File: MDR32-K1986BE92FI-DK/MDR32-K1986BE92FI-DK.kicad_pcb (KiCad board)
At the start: 2 copper layers, 69.6 x 21.4 mm, 57 parts, among them J1 Conn_PROBE, J2 PIN_A, J3 SYS_A, J4 USB_C_Receptacle_USB2.0_16P, J5 PIN_B, J6 SYS_B, Q1 AO3401A, SW1 IT-1181, SW2 SW_DIP_x02, SW3 IT-1181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

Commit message: fix position
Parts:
- moved R1 95.9 mm to (154.5, 134.9)
- moved R2 72.1 mm to (128.7, 134.8)
- moved SW1 57.9 mm to (145.4, 130.8)
- moved Q1 54.1 mm to (147.2, 136.4)
- moved U1 53.5 mm to (125.9, 104.9)
- moved D3 40.0 mm to (128.7, 137.9)
- moved C2 39.4 mm to (118.2, 119.3)
- moved C1 39.2 mm to (118.3, 114.7)
- moved D1 38.3 mm to (128.2, 113.3)
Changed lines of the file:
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@@
 	(footprint "Capacitor_SMD:C_0805_2012Metric"
 		(layer "F.Cu")
-		(at 80.39 104.995)
+		(at 118.35 114.67)
 		(descr "Capacitor SMD 0805 (2012 Metric), square (rectangular) end terminal, IPC_7351 nominal, (Body size source: IPC-SM-782 page 76, https://www.pcb-3d.com/wordpress/wp-content/uploads/ipc-sm-782a_amendment_1_and_2.pdf, https://docs.google.com/spreadsheets/d/1BsfQQcO9C6DZCsRaXUlFlo91Tg2WpOkGARC1WS5S8t0/edit?usp=sharing), generated with kicad-footprint-generator")
 		(tags "capacitor")
@@
 	(footprint "Resistor_SMD:R_0603_1608Metric"
 		(layer "F.Cu")
-		(at 68.14 95.725)
+		(at 128.685 134.81)
 		(descr "Resistor SMD 0603 (1608 Metric), square (rectangular) end terminal, IPC_7351 nominal, (Body size source: IPC-SM-782 page 72, https://www.pcb-3d.com/wordpress/wp-content/uploads/ipc-sm-782a_amendment_1_and_2.pdf), generated with kicad-footprint-generator")
 		(tags "resistor")
@@
 	(footprint "Package_TO_SOT_SMD:SOT-223-3_TabPin2"
 		(layer "F.Cu")
-		(at 76.35 125)
+		(at 125.93 104.9)
 		(descr "module CMS SOT223 4 pins")
 		(tags "CMS SOT")
@@
 	(footprint "Button_Switch_SMD:SW_SPST_CK_RS282G05A3"
 		(layer "F.Cu")
-		(at 88.12 122.095)
+		(at 145.39 130.82)
 		(descr "https://www.mouser.com/ds/2/60/RS-282G05A-SM_RT-1159762.pdf")
 		(tags "SPST button tactile switch")
@@
 		(locked yes)
 		(layer "F.Cu")
-		(at 20.72 27.73 -90)
+		(at 20.715 27.73 -90)
 		(descr "USB 2.0 Type C Receptacle, GCT, 16P, top mounted, horizontal, 5A: https://gct.co/files/drawings/usb4105.pdf")
 		(tags "USB C Type-C Receptacle SMD USB 2.0 16P 16C USB4105-15-A USB4105-15-A-060 USB4105-15-A-120 USB4105-GF-A USB4105-GF-A-060 USB4105-GF-A-120")
@@
 	(footprint "Resistor_SMD:R_0603_1608Metric"
 		(layer "F.Cu")
-		(at 68.14 93.215)
+		(at 154.535 134.9)
 		(descr "Resistor SMD 0603 (1608 Metric), square (rectangular) end terminal, IPC_7351 nominal, (Body size source: IPC-SM-782 page 72, https://www.pcb-3d.com/wordpress/wp-content/uploads/ipc-sm-782a_amendment_1_and_2.pdf), generated with kicad-footprint-generator")
 		(tags "resistor")
@@
 	(footprint "Capacitor_SMD:C_0805_2012Metric"
 		(layer "F.Cu")
-		(at 80.39 108.005)
+		(at 118.16 119.29)
 		(descr "Capacitor SMD 0805 (2012 Metric), square (rectangular) end terminal, IPC_7351 nominal, (Body size source: IPC-SM-782 page 76, https://www.pcb-3d.com/wordpress/wp-content/uploads/ipc-sm-782a_amendment_1_and_2.pdf, https://docs.google.com/spreadsheets/d/1BsfQQcO9C6DZCsRaXUlFlo91Tg2WpOkGARC1WS5S8t0/edit?usp=sharing), generated with kicad-footprint-generator")
 		(tags "capacitor")
@@
 	(footprint "LED_SMD:LED_0805_2012Metric"
 		(layer "F.Cu")
-		(at 89.29 131.34)
+		(at 128.74 137.9)
 		(descr "LED SMD 0805 (2012 Metric), square (rectangular) end terminal, IPC_7351 nominal, (Body size source: https://docs.google.com/spreadsheets/d/1BsfQQcO9C6DZCsRaXUlFlo91Tg2WpOkGARC1WS5S8t0/edit?usp=sharing), generated with kicad-footprint-generator")
 		(tags "LED")
@@
 	(footprint "Diode_SMD:D_SOD-123"
 		(layer "F.Cu")
-		(at 90.785 105.165)
+		(at 128.21 113.26)
 		(descr "SOD-123")
 		(tags "SOD-123")
@@
 	(footprint "Package_TO_SOT_SMD:SOT-23"
 		(layer "F.Cu")
-		(at 96.83 116.555)
+		(at 147.1725 136.41)
 		(descr "SOT, 3 Pin (JEDEC TO-236 Var AB https://www.jedec.org/document_search?search_api_views_fulltext=TO-236), generated with kicad-footprint-generator ipc_gullwing_generator.py")
 		(tags "SOT TO_SOT_SMD")

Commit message: update footprints
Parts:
- J1: footprint Connector_PinHeader_2.54mm:PinHeader_1x04_P2.54mm_Vertical -> Connector_PinHeader_2.54mm:PinHeader_1x04_P2.54mm_Horizontal
- SW1, SW3: footprint Button_Switch_SMD:SW_SPST_CK_RS282G05A3 -> Button_Switch_SMD:SW_SPST_B3U-1000P

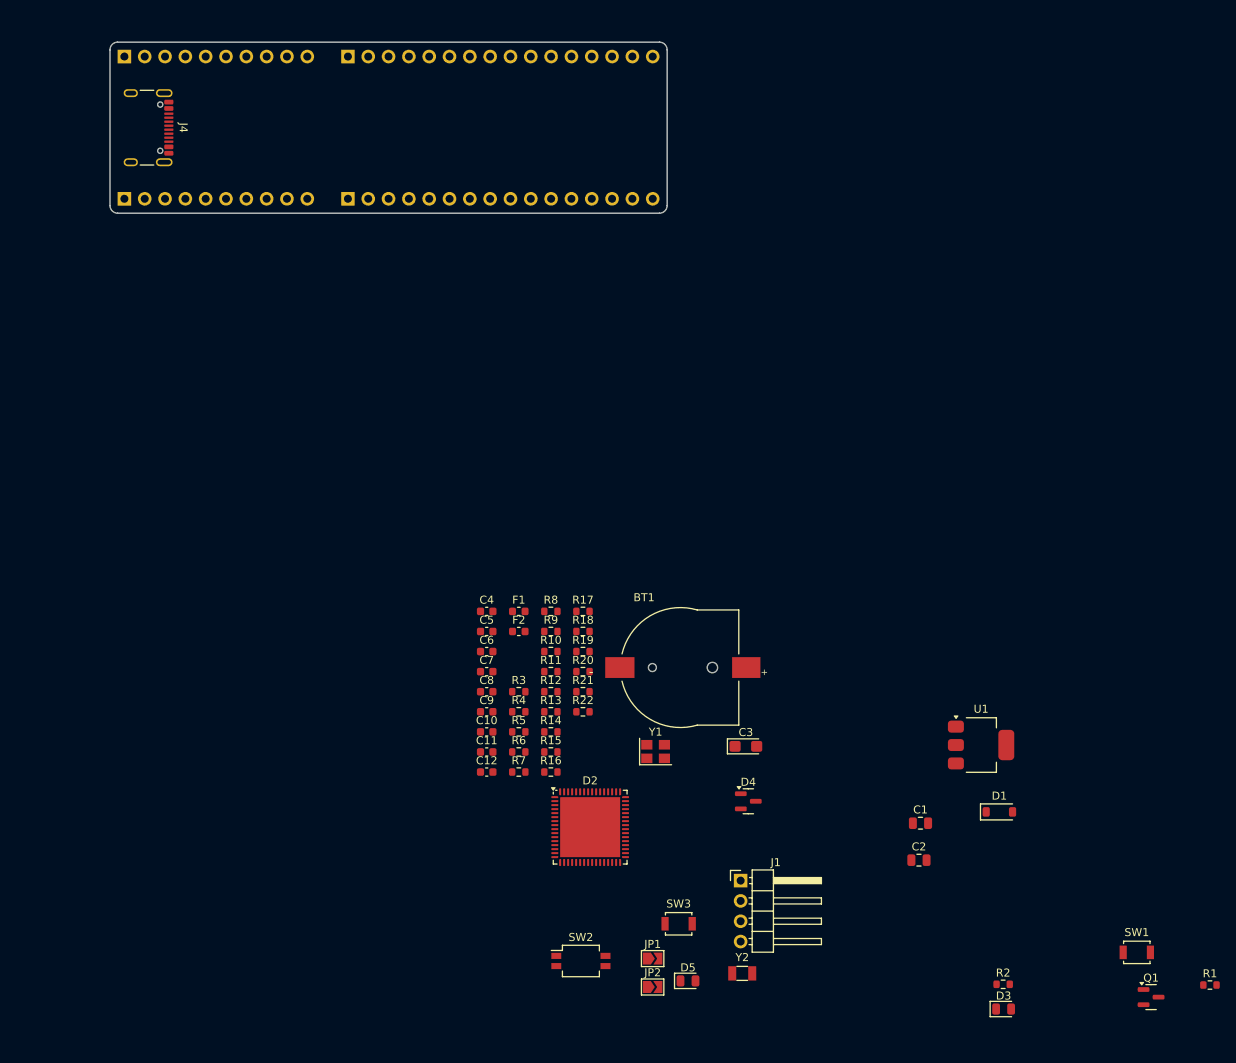
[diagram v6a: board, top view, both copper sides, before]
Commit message: position SW pinout
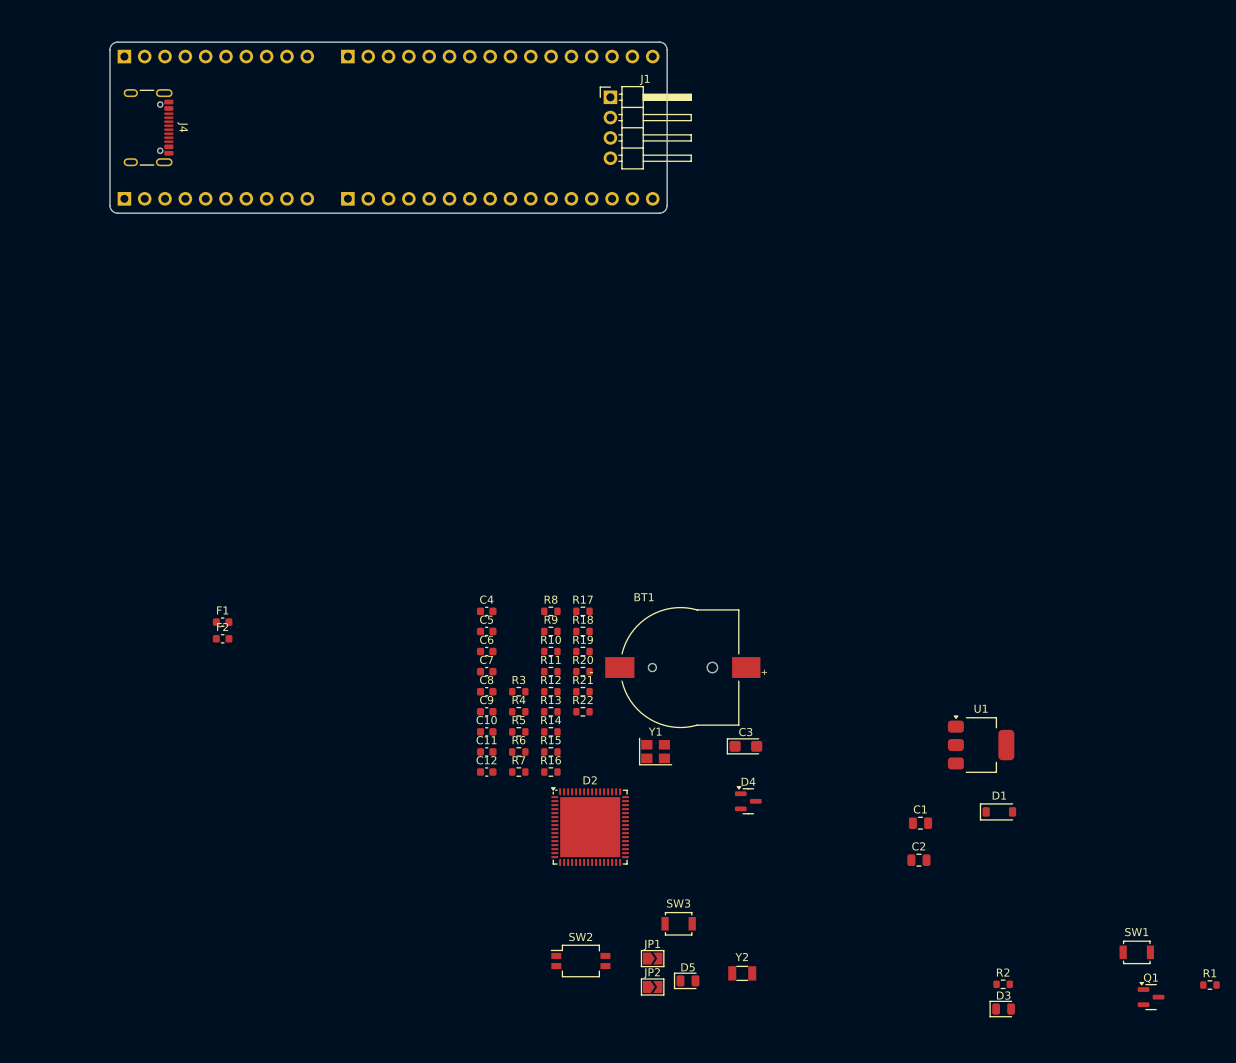
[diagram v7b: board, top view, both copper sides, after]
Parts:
- moved J1 99.3 mm to (79.6, 23.9)
- moved F1 37.0 mm to (31.1, 89.5)
- moved F2 37.0 mm to (31.1, 91.6)
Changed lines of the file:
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@@
 	(footprint "Fuse:Fuse_0603_1608Metric"
 		(layer "F.Cu")
-		(at 68.14 88.195)
+		(at 31.12 89.54)
 		(descr "Fuse SMD 0603 (1608 Metric), square (rectangular) end terminal, IPC_7351 nominal, (Body size source: http://www.tortai-tech.com/upload/download/2011102023233369053.pdf), generated with kicad-footprint-generator")
 		(tags "fuse")
@@
 	(footprint "Fuse:Fuse_0603_1608Metric"
 		(layer "F.Cu")
-		(at 68.14 90.705)
+		(at 31.1225 91.62)
 		(descr "Fuse SMD 0603 (1608 Metric), square (rectangular) end terminal, IPC_7351 nominal, (Body size source: http://www.tortai-tech.com/upload/download/2011102023233369053.pdf), generated with kicad-footprint-generator")
 		(tags "fuse")
@@
 	)
 	(footprint "Connector_PinHeader_2.54mm:PinHeader_1x04_P2.54mm_Horizontal"
+		(locked yes)
 		(layer "F.Cu")
-		(at 95.87 121.845)
+		(at 79.595 23.93)
 		(descr "Through hole angled pin header, 1x04, 2.54mm pitch, 6mm pin length, single row")
 		(tags "Through hole angled pin header THT 1x04 2.54mm single row")

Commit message: part made
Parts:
- C1, C2, D1, D4, U1: moved to B.Cu
- C10, C11, C12, C4, C5, C6, C7, C8, C9: footprint Capacitor_SMD:C_0603_1608Metric -> Capacitor_SMD:C_0402_1005Metric
- D3, D5: footprint LED_SMD:LED_0805_2012Metric -> LED_SMD:LED_0603_1608Metric
- R1, R10, R11, R12, R13, R14, R15, R16, R17, R18, R19, R2, R20, R21, R22, R3, R4, R5, R6, R7, R8, R9: footprint Resistor_SMD:R_0603_1608Metric -> Resistor_SMD:R_0402_1005Metric
- moved R1 158.8 mm to (35.0, 30.3)
- moved Q1 156.6 mm to (34.0, 28.1), turned to 180 degrees
- moved SW1 147.3 mm to (35.8, 32.4)
- moved C1 143.4 mm to (6.76, 24.6), turned to 180 degrees
- moved D3 142.6 mm to (32.6, 32.6), turned to -90 degrees
- moved R2 141.7 mm to (33.0, 30.3)
- moved D1 141.1 mm to (11.5, 34.0)
- moved C2 140.4 mm to (6.74, 33.8), turned to 180 degrees
- moved U1 138.9 mm to (9.46, 29.2)
- moved D5 124.4 mm to (32.6, 23.7), turned to -90 degrees
- moved SW3 115.9 mm to (35.8, 23.8), turned to 180 degrees
- moved SW2 113.4 mm to (29.6, 28.4), turned to -90 degrees
- moved D4 99.0 mm to (27.9, 40.9)
- moved D2 93.2 mm to (44.2, 27.9), turned to -135 degrees
- moved R21 89.5 mm to (26.2, 24.0), turned to 90 degrees
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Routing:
- net /USBDN: track 0.00 -> 3.08 mm
- net /USBDP: track 0.00 -> 2.81 mm
